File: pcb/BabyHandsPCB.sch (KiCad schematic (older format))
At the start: 44 parts

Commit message: Route matrix
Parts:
- MX1, MX10, MX11, MX12, MX13, MX14, MX15, MX16, MX17, MX19, MX2, MX20, MX21, MX3, MX4, MX5, MX6, MX7, MX8, MX9: footprint kbd:MX_ALPS_PG1350_noLed -> kbd:CherryMX_Choc_Hotswap
- MX18, MX22: footprint kbd:MX_ALPS_PG1350_noLed_1.75u -> kbd:CherryMX_Choc_Hotswap_1.5u
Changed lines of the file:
@@
 EESchema Schematic File Version 4
+LIBS:BabyHandsPCB-cache
 EELAYER 30 0
 EELAYER END
@@
 F 0 "MX1" H 6733 1623 60  0000 C CNN
 F 1 "MX-NoLED" H 6733 1549 20  0000 C CNN
-F 2 "kbd:MX_ALPS_PG1350_noLed" H 6075 1375 60  0001 C CNN
+F 2 "kbd:CherryMX_Choc_Hotswap" H 6075 1375 60  0001 C CNN
 F 3 "" H 6075 1375 60  0001 C CNN
 	1    6700 1400
@@
 F 0 "MX4" H 7383 1623 60  0000 C CNN
 F 1 "MX-NoLED" H 7383 1549 20  0000 C CNN
-F 2 "kbd:MX_ALPS_PG1350_noLed" H 6725 1375 60  0001 C CNN
+F 2 "kbd:CherryMX_Choc_Hotswap" H 6725 1375 60  0001 C CNN
 F 3 "" H 6725 1375 60  0001 C CNN
 	1    7350 1400
@@
 F 0 "MX7" H 8033 1623 60  0000 C CNN
 F 1 "MX-NoLED" H 8033 1549 20  0000 C CNN
-F 2 "kbd:MX_ALPS_PG1350_noLed" H 7375 1375 60  0001 C CNN
+F 2 "kbd:CherryMX_Choc_Hotswap" H 7375 1375 60  0001 C CNN
 F 3 "" H 7375 1375 60  0001 C CNN
 	1    8000 1400
@@
 F 0 "MX11" H 8683 1623 60  0000 C CNN
 F 1 "MX-NoLED" H 8683 1549 20  0000 C CNN
-F 2 "kbd:MX_ALPS_PG1350_noLed" H 8025 1375 60  0001 C CNN
+F 2 "kbd:CherryMX_Choc_Hotswap" H 8025 1375 60  0001 C CNN
 F 3 "" H 8025 1375 60  0001 C CNN
 	1    8650 1400
@@
 F 0 "MX15" H 9333 1623 60  0000 C CNN
 F 1 "MX-NoLED" H 9333 1549 20  0000 C CNN
-F 2 "kbd:MX_ALPS_PG1350_noLed" H 8675 1375 60  0001 C CNN
+F 2 "kbd:CherryMX_Choc_Hotswap" H 8675 1375 60  0001 C CNN
 F 3 "" H 8675 1375 60  0001 C CNN
 	1    9300 1400
@@
 F 0 "MX19" H 9983 1623 60  0000 C CNN
 F 1 "MX-NoLED" H 9983 1549 20  0000 C CNN
-F 2 "kbd:MX_ALPS_PG1350_noLed" H 9325 1375 60  0001 C CNN
+F 2 "kbd:CherryMX_Choc_Hotswap" H 9325 1375 60  0001 C CNN
 F 3 "" H 9325 1375 60  0001 C CNN
 	1    9950 1400
@@
 F 0 "MX2" H 6733 2423 60  0000 C CNN
 F 1 "MX-NoLED" H 6733 2349 20  0000 C CNN
-F 2 "kbd:MX_ALPS_PG1350_noLed" H 6075 2175 60  0001 C CNN
+F 2 "kbd:CherryMX_Choc_Hotswap" H 6075 2175 60  0001 C CNN
 F 3 "" H 6075 2175 60  0001 C CNN
 	1    6700 2200
@@
 F 0 "MX5" H 7383 2423 60  0000 C CNN
 F 1 "MX-NoLED" H 7383 2349 20  0000 C CNN
-F 2 "kbd:MX_ALPS_PG1350_noLed" H 6725 2175 60  0001 C CNN
+F 2 "kbd:CherryMX_Choc_Hotswap" H 6725 2175 60  0001 C CNN
 F 3 "" H 6725 2175 60  0001 C CNN
 	1    7350 2200
@@
 F 0 "MX8" H 8033 2423 60  0000 C CNN
 F 1 "MX-NoLED" H 8033 2349 20  0000 C CNN
-F 2 "kbd:MX_ALPS_PG1350_noLed" H 7375 2175 60  0001 C CNN
+F 2 "kbd:CherryMX_Choc_Hotswap" H 7375 2175 60  0001 C CNN
 F 3 "" H 7375 2175 60  0001 C CNN
 	1    8000 2200
@@
 F 0 "MX12" H 8683 2423 60  0000 C CNN
 F 1 "MX-NoLED" H 8683 2349 20  0000 C CNN
-F 2 "kbd:MX_ALPS_PG1350_noLed" H 8025 2175 60  0001 C CNN
+F 2 "kbd:CherryMX_Choc_Hotswap" H 8025 2175 60  0001 C CNN
 F 3 "" H 8025 2175 60  0001 C CNN
 	1    8650 2200
@@
 F 0 "MX16" H 9333 2423 60  0000 C CNN
 F 1 "MX-NoLED" H 9333 2349 20  0000 C CNN
-F 2 "kbd:MX_ALPS_PG1350_noLed" H 8675 2175 60  0001 C CNN
+F 2 "kbd:CherryMX_Choc_Hotswap" H 8675 2175 60  0001 C CNN
 F 3 "" H 8675 2175 60  0001 C CNN
 	1    9300 2200
@@
 F 0 "MX20" H 9983 2423 60  0000 C CNN
 F 1 "MX-NoLED" H 9983 2349 20  0000 C CNN
-F 2 "kbd:MX_ALPS_PG1350_noLed" H 9325 2175 60  0001 C CNN
+F 2 "kbd:CherryMX_Choc_Hotswap" H 9325 2175 60  0001 C CNN
 F 3 "" H 9325 2175 60  0001 C CNN
 	1    9950 2200
@@
 F 0 "MX3" H 6733 3223 60  0000 C CNN
 F 1 "MX-NoLED" H 6733 3149 20  0000 C CNN
-F 2 "kbd:MX_ALPS_PG1350_noLed" H 6075 2975 60  0001 C CNN
+F 2 "kbd:CherryMX_Choc_Hotswap" H 6075 2975 60  0001 C CNN
 F 3 "" H 6075 2975 60  0001 C CNN
 	1    6700 3000
@@
 F 0 "MX6" H 7383 3223 60  0000 C CNN
 F 1 "MX-NoLED" H 7383 3149 20  0000 C CNN
-F 2 "kbd:MX_ALPS_PG1350_noLed" H 6725 2975 60  0001 C CNN
+F 2 "kbd:CherryMX_Choc_Hotswap" H 6725 2975 60  0001 C CNN
 F 3 "" H 6725 2975 60  0001 C CNN
 	1    7350 3000
@@
 F 0 "MX9" H 8033 3223 60  0000 C CNN
 F 1 "MX-NoLED" H 8033 3149 20  0000 C CNN
-F 2 "kbd:MX_ALPS_PG1350_noLed" H 7375 2975 60  0001 C CNN
+F 2 "kbd:CherryMX_Choc_Hotswap" H 7375 2975 60  0001 C CNN
 F 3 "" H 7375 2975 60  0001 C CNN
 	1    8000 3000
@@
 F 0 "MX13" H 8683 3223 60  0000 C CNN
 F 1 "MX-NoLED" H 8683 3149 20  0000 C CNN
-F 2 "kbd:MX_ALPS_PG1350_noLed" H 8025 2975 60  0001 C CNN
+F 2 "kbd:CherryMX_Choc_Hotswap" H 8025 2975 60  0001 C CNN
 F 3 "" H 8025 2975 60  0001 C CNN
 	1    8650 3000
@@
 F 0 "MX17" H 9333 3223 60  0000 C CNN
 F 1 "MX-NoLED" H 9333 3149 20  0000 C CNN
-F 2 "kbd:MX_ALPS_PG1350_noLed" H 8675 2975 60  0001 C CNN
+F 2 "kbd:CherryMX_Choc_Hotswap" H 8675 2975 60  0001 C CNN
 F 3 "" H 8675 2975 60  0001 C CNN
 	1    9300 3000
@@
 F 0 "MX21" H 9983 3223 60  0000 C CNN
 F 1 "MX-NoLED" H 9983 3149 20  0000 C CNN
-F 2 "kbd:MX_ALPS_PG1350_noLed" H 9325 2975 60  0001 C CNN
+F 2 "kbd:CherryMX_Choc_Hotswap" H 9325 2975 60  0001 C CNN
 F 3 "" H 9325 2975 60  0001 C CNN
 	1    9950 3000
@@
 F 0 "MX10" H 8033 4023 60  0000 C CNN
 F 1 "MX-NoLED" H 8033 3949 20  0000 C CNN
-F 2 "kbd:MX_ALPS_PG1350_noLed" H 7375 3775 60  0001 C CNN
+F 2 "kbd:CherryMX_Choc_Hotswap" H 7375 3775 60  0001 C CNN
 F 3 "" H 7375 3775 60  0001 C CNN
 	1    8000 3800
@@
 F 0 "MX14" H 8683 4023 60  0000 C CNN
 F 1 "MX-NoLED" H 8683 3949 20  0000 C CNN
-F 2 "kbd:MX_ALPS_PG1350_noLed" H 8025 3775 60  0001 C CNN
+F 2 "kbd:CherryMX_Choc_Hotswap" H 8025 3775 60  0001 C CNN
 F 3 "" H 8025 3775 60  0001 C CNN
 	1    8650 3800
@@
 F 0 "MX18" H 9333 4023 60  0000 C CNN
 F 1 "MX-NoLED" H 9333 3949 20  0000 C CNN
-F 2 "kbd:MX_ALPS_PG1350_noLed_1.75u" H 8675 3775 60  0001 C CNN
+F 2 "kbd:CherryMX_Choc_Hotswap_1.5u" H 8675 3775 60  0001 C CNN
 F 3 "" H 8675 3775 60  0001 C CNN
 	1    9300 3800
@@
 F 0 "MX22" H 9983 4023 60  0000 C CNN
 F 1 "MX-NoLED" H 9983 3949 20  0000 C CNN
-F 2 "kbd:MX_ALPS_PG1350_noLed_1.75u" H 9325 3775 60  0001 C CNN
+F 2 "kbd:CherryMX_Choc_Hotswap_1.5u" H 9325 3775 60  0001 C CNN
 F 3 "" H 9325 3775 60  0001 C CNN
 	1    9950 3800

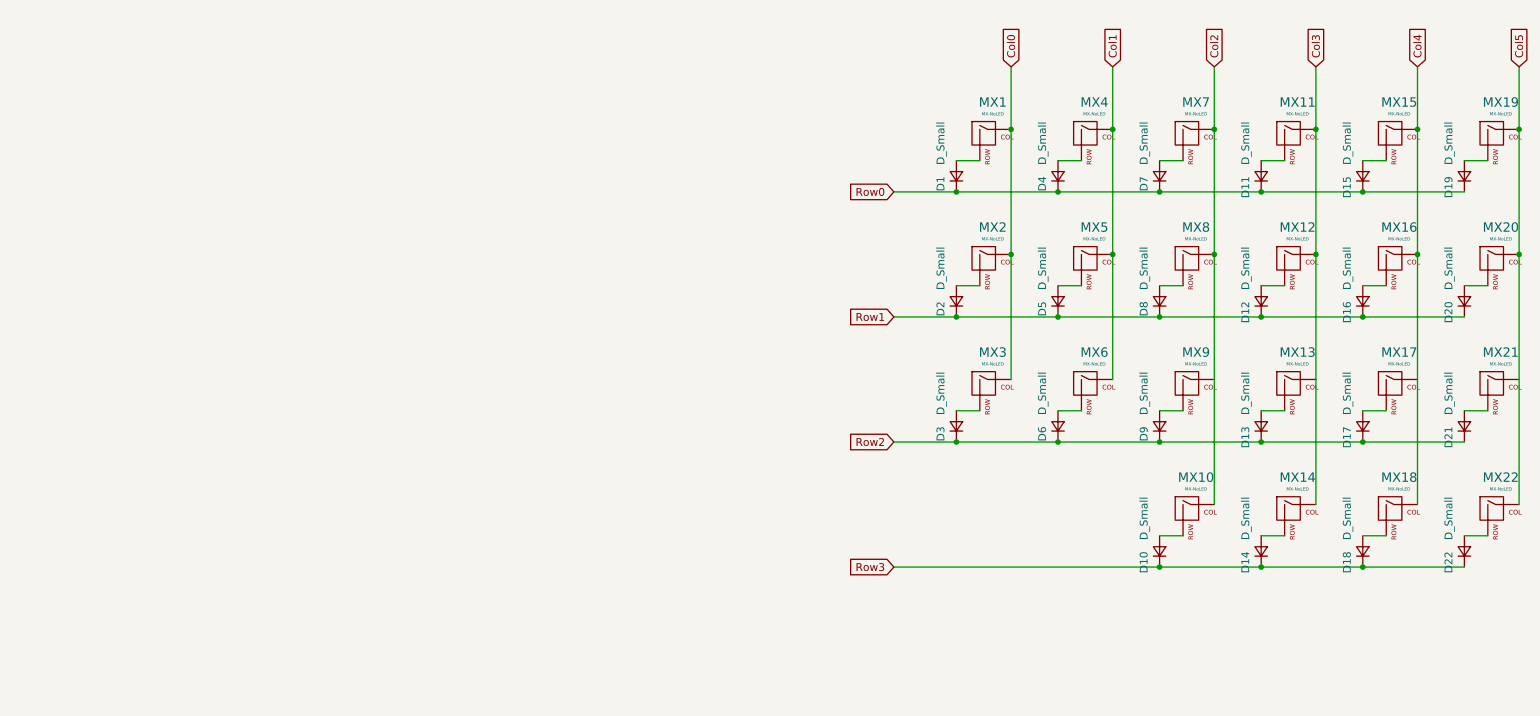
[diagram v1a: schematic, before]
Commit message: Add pro micro
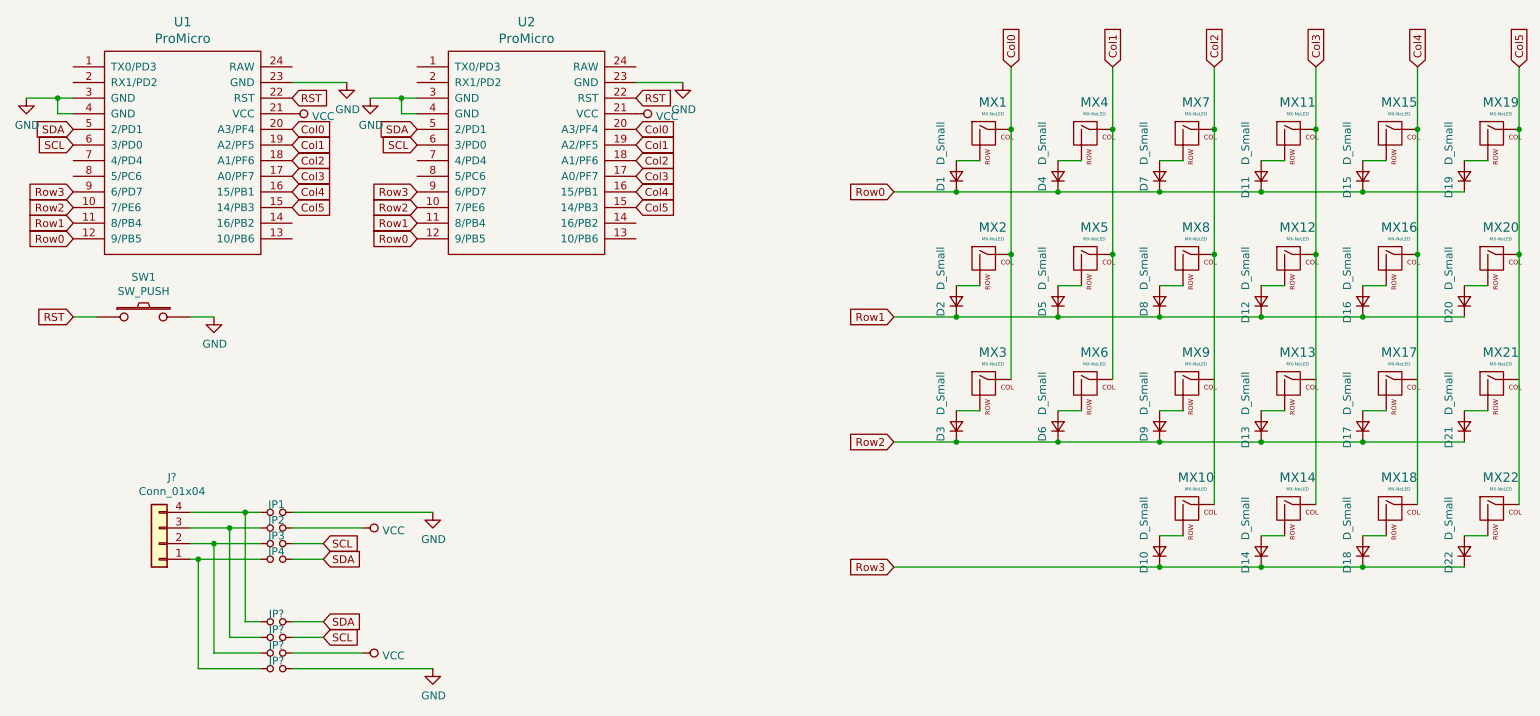
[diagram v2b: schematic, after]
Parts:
- added J?: Conn_01x04, symbol Connector_Generic:Conn_01x04
- added JP1, JP2, JP3, JP4, JP? (x4): Jumper_NO_Small, kbd:Jumper, symbol Device:Jumper_NO_Small
- added SW1: SW_PUSH, Button_Switch_THT:SW_Tactile_SPST_Angled_PTS645Vx31-2LFS, symbol kbd:SW_PUSH
- added U1, U2: ProMicro, Keebio-Parts:ArduinoProMicro-BackSide, symbol keebio:ProMicro
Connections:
- net Col0: now also U1.20 (A3/PF4), U2.20 (A3/PF4)
- net Col1: now also U1.19 (A2/PF5), U2.19 (A2/PF5)
- net Col2: now also U1.18 (A1/PF6), U2.18 (A1/PF6)
- net Col3: now also U1.17 (A0/PF7), U2.17 (A0/PF7)
- net Col4: now also U1.16 (15/PB1), U2.16 (15/PB1)
- net Col5: now also U1.15 (14/PB3), U2.15 (14/PB3)
- net Row0: now also U1.12 (9/PB5), U2.12 (9/PB5)
- net Row1: now also U1.11 (8/PB4), U2.11 (8/PB4)
- net Row2: now also U1.10 (7/PE6), U2.10 (7/PE6)
- net Row3: now also U1.9 (6/PD7), U2.9 (6/PD7)
- new net: J?.4 (Pin_4), JP1.1, JP?.1
- new net: J?.3 (Pin_3), JP2.1, JP?.1
- new net: J?.2 (Pin_2), JP3.1, JP?.1
- new net: J?.1 (Pin_1), JP4.1, JP?.1
- new net GND: JP1.2, JP?.2, SW1.2, U1.23 (GND), U1.3 (GND), U1.4 (GND), U2.23 (GND), U2.3 (GND), U2.4 (GND)
- new net RST: SW1.1, U1.22 (RST), U2.22 (RST)
- new net SCL: JP3.2, JP?.2, U1.6 (3/PD0), U2.6 (3/PD0)
- new net SDA: JP4.2, JP?.2, U1.5 (2/PD1), U2.5 (2/PD1)
- new net VCC: JP2.2, JP?.2, U1.21 (VCC), U2.21 (VCC)
